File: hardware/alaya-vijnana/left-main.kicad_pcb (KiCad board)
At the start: 4 copper layers, 113.1 x 85.8 mm, 77 parts, among them J1 Bat, J2 USB_C_Receptacle_USB2.0_16P, J5 MAIN_CONN, SW1 Power_Switch, SW10 MX HotSwap, SW11 MX HotSwap, SW12 MX HotSwap, SW13 MX HotSwap, SW14 MX HotSwap, SW15 MX HotSwap, SW16 MX HotSwap, SW2 MX HotSwap, SW3 MX HotSwap, SW4 MX HotSwap, SW5 MX HotSwap, SW6 MX HotSwap, SW7 MX HotSwap, SW8 MX HotSwap, SW9 MX HotSwap, U1 nRF52840, U2 BQ24075RGT, U3 XC6220B331MR, X1 32.768kHz, Y1 32Mhz

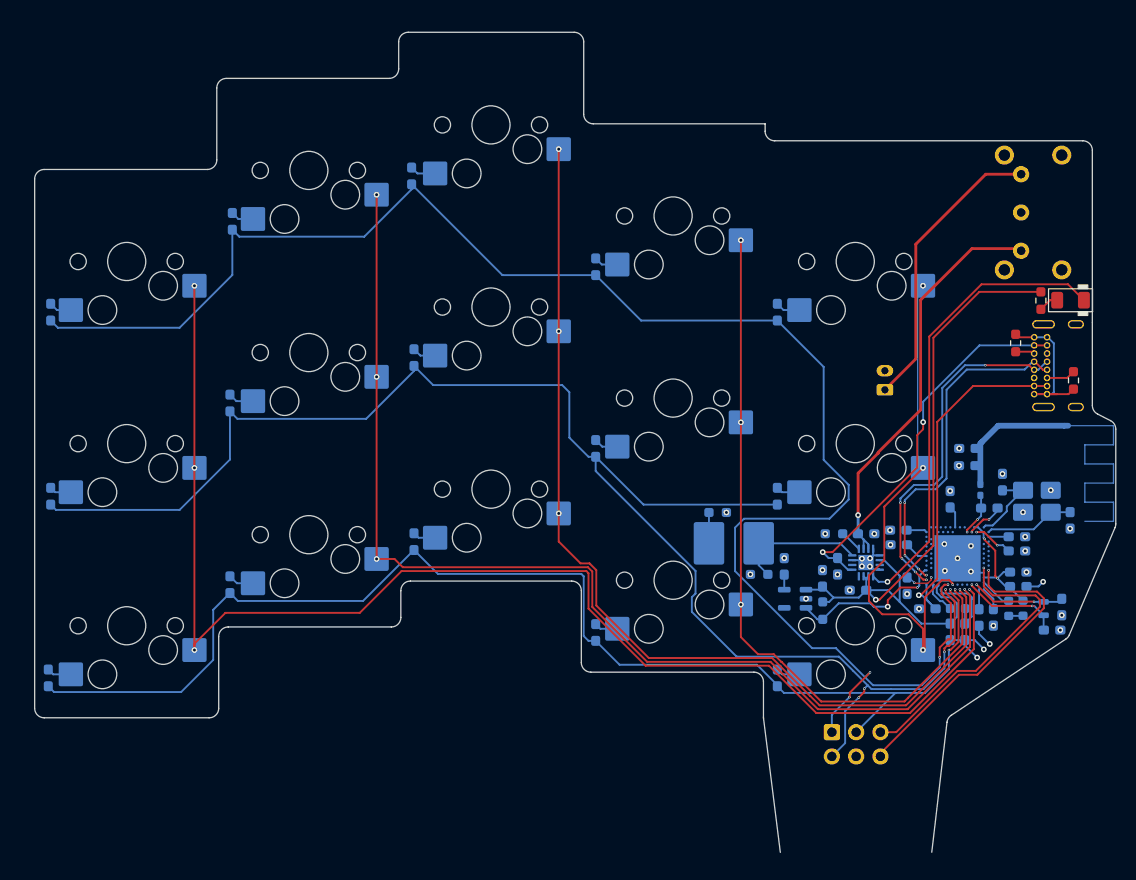
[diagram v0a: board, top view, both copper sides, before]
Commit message: added firmware
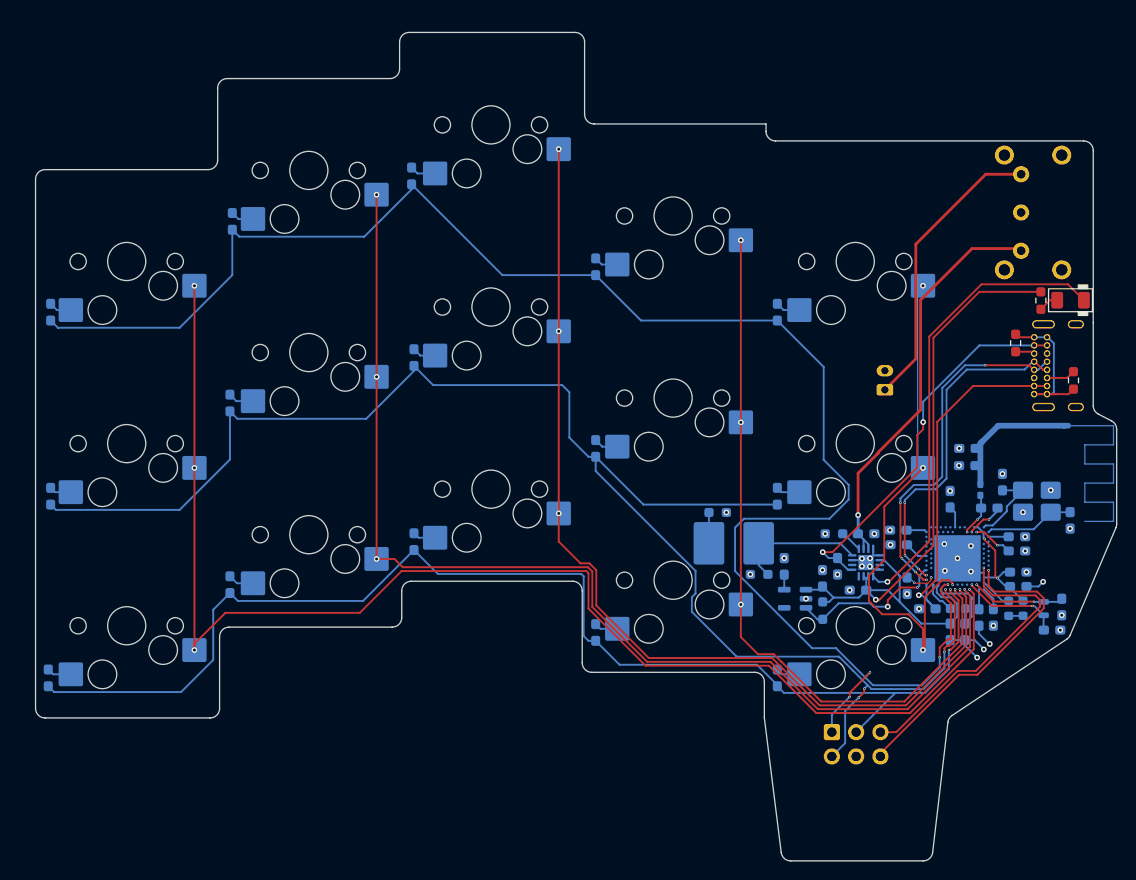
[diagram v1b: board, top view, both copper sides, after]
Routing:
- added copper zone on In2.Cu, net L_BAT-
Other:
- board size 113.1 x 85.8 mm -> 113.1 x 86.7 mm
- board text added: "JLCJLCJLCJLC"
- board text removed: "JLCJLCJLC"

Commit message: production stuff
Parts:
- added SW45: SW_Push, Button_Switch_SMD:SW_Push_1P1T_NO_CK_KMR2, F.Cu at (184.2, 60.0)
- moved C1 2.09 mm to (187.8, 92.2)
- moved J5 2.09 mm to (170.0, 118.3)
- moved L1 2.09 mm to (185.5, 93.0)
- moved R6 2.09 mm to (189.2, 77.6)
- moved SW14 2.09 mm to (172.4, 69.1)
- moved SW15 2.09 mm to (172.4, 88.2)
- moved U3 2.09 mm to (166.1, 104.4)
- moved C24 2.09 mm to (193.0, 107.7)
- moved C3 2.09 mm to (170.5, 101.0)
- moved C6 2.09 mm to (186.4, 94.9)
- moved C7 2.09 mm to (184.1, 90.5)
- moved J2 2.09 mm to (191.1, 77.0)
- moved R3 2.09 mm to (170.2, 97.6)
- moved SW16 2.09 mm to (172.4, 107.2)
- moved SW2 2.09 mm to (96.2, 69.1)
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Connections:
- U1 pad AC13: unconnected-(U1-P0.18/~{RESET}-PadAC13) -> Net-(U1-P0.18/~{RESET})
- Y1 pad 4: L_BAT- -> (no net)
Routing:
- net Net-(U1-P0.18/~{RESET}): track 0.00 -> 48.3 mm, vias 0 -> 3
- net L_BAT-: track 42.5 -> 46.6 mm, vias 41 -> 43
- net L_BAT+: track 30.6 -> 28.5 mm
- net L_D+: track 35.6 -> 34.0 mm, vias 4 -> 2
- net L_D-: track 36.9 -> 35.4 mm, vias 5 -> 2
- removed copper zone on In2.Cu, net L_BAT-
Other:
- outline, holes or cut-outs redrawn
- board text added: "JLCJLCJLC"
- board text removed: "JLCJLCJLCJLC"
